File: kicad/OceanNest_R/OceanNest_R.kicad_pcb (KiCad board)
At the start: 2 copper layers, 103.4 x 85.9 mm, 40 parts, among them J21 Conn_01x07_Pin, J22 TRRS_MJ-4PP-9, SW21 SW_PUSH, SW22 SW_PUSH, SW23 SW_PUSH, SW24 SW_PUSH, SW25 SW_PUSH, SW26 SW_PUSH, SW27 SW_PUSH, SW28 SW_PUSH, SW29 SW_PUSH, SW30 SW_PUSH, SW31 SW_PUSH, SW32 SW_PUSH, SW33 SW_PUSH, SW34 SW_PUSH, SW35 SW_PUSH, SW36 SW_PUSH, U21 RP2040-Zero

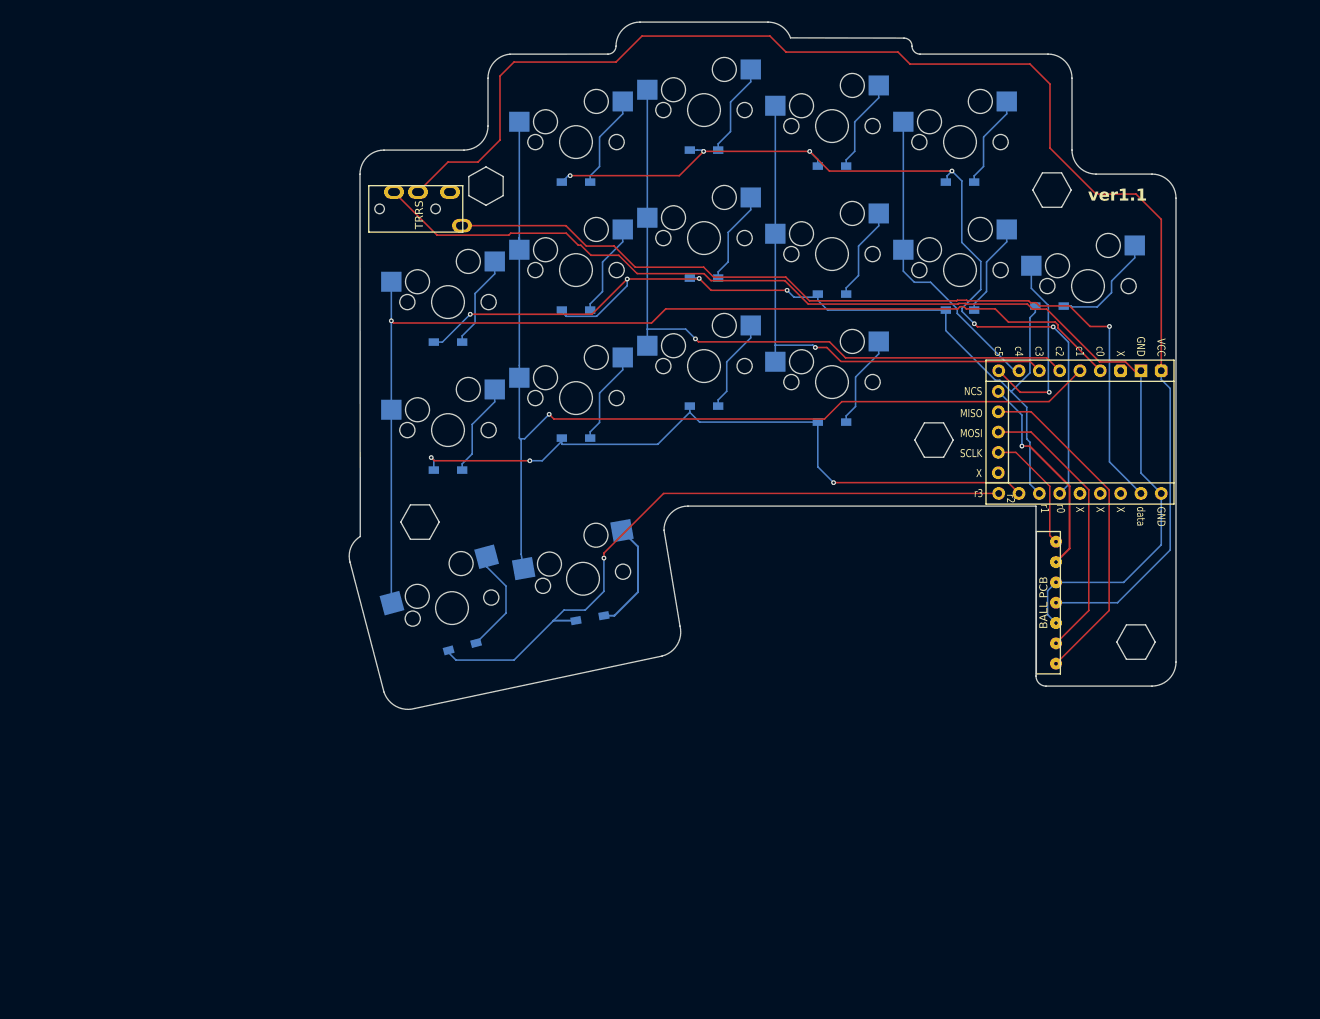
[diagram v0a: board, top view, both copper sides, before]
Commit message: feat: update PCB and schematic files for OceanNest project, including new components and layout adjustments
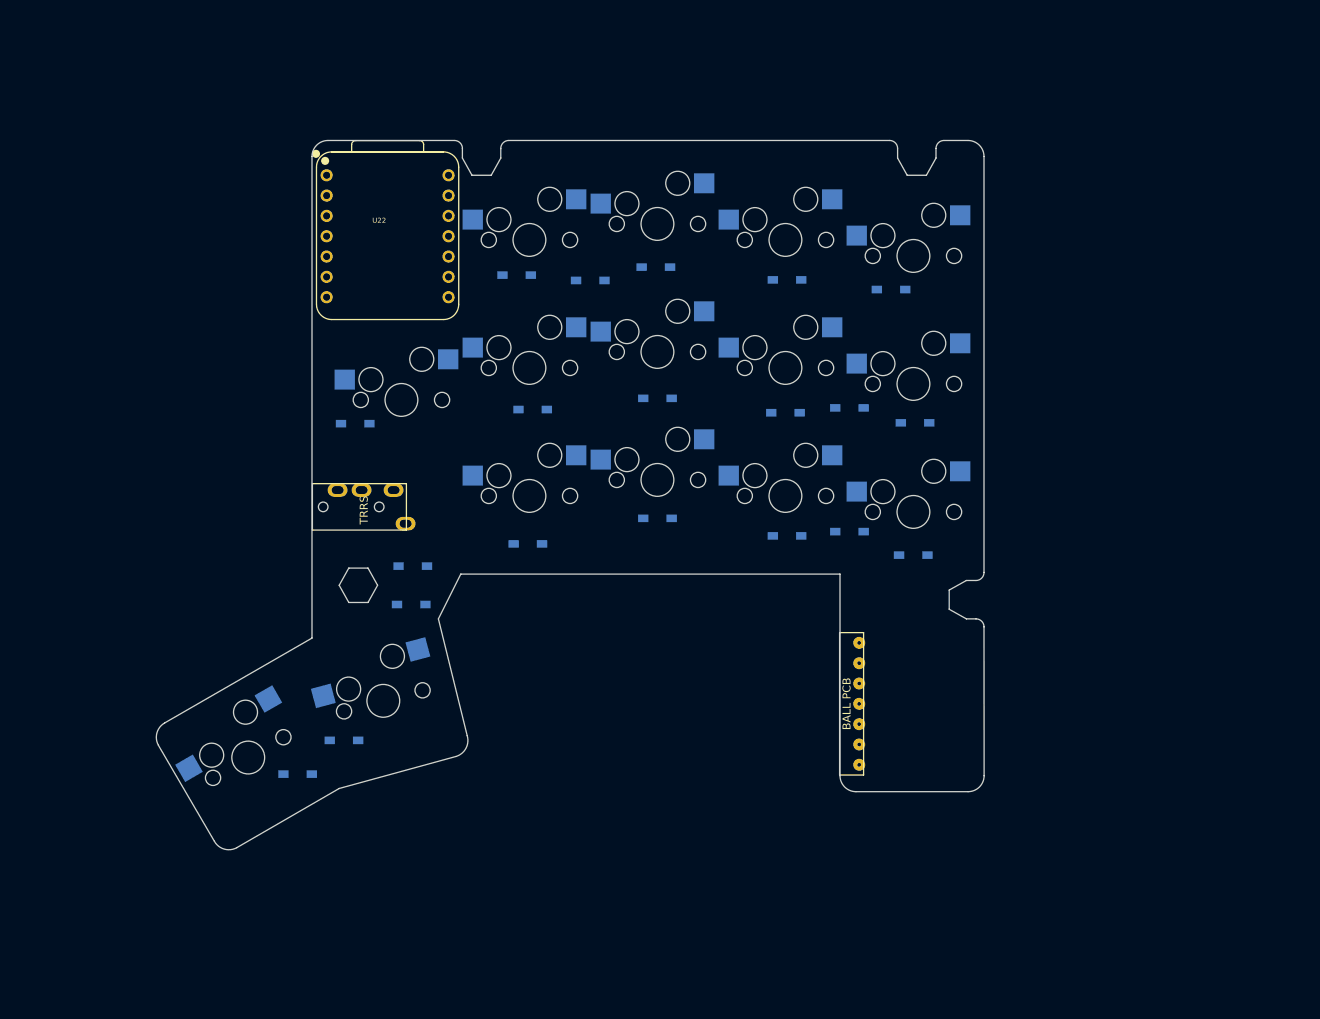
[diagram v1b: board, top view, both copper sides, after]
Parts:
- removed the Ref** at (197.0, 124.5)
- removed the Ref** at (115.8, 67.5)
- removed the Ref** at (171.8, 99.2)
- removed the Ref** at (107.5, 109.5)
- removed the Ref** at (186.5, 68.0)
- removed SW36: SW_PUSH, takashicompany:CherryMX_Hotswap_16m
- removed U21: RP2040-Zero, isw-kbd:RP2040-Zero
- added D37: D, kbd_Parts:Diode_SMD, F.Cu at (169.2, 113.6)
- added D38: D, kbd_Parts:Diode_SMD, F.Cu at (92.2, 141.0)
- added D39: D, kbd_Parts:Diode_SMD, F.Cu at (98.0, 136.8)
- added D40: D, kbd_Parts:Diode_SMD, F.Cu at (106.6, 115.0)
- added Ref**: Val**, kbd_Hole:m2_Spacer_Hole_hex, F.Cu at (99.8, 117.4)
- added U22: XIAO-RP2040-TH, xiao_rp2040:XIAO-RP2040-TH, F.Cu at (103.5, 73.8)
- J21: value Conn_01x07_Pin -> TRRS_MJ-4PP-9; footprint kbd:Mac8_L_7pin_contact_NEW2023 -> kbd:MJ-4PP-9; moved to F.Cu
- J22: value TRRS_MJ-4PP-9 -> Conn_01x07_Pin; footprint kbd:MJ-4PP-9 -> kbd:Mac8_L_7pin_contact_NEW2023; moved to B.Cu
- SW21, SW22, SW23, SW24, SW25, SW26, SW27, SW28, SW29, SW30, SW31, SW32, SW33, SW34, SW35: value SW_PUSH -> SW_Push
- moved J21 94.1 mm to (93.9, 107.6)
- moved J22 87.3 mm to (162.6, 132.2)
- moved SW34 86.8 mm to (86.0, 138.9), turned to 30 degrees
- moved SW30 74.6 mm to (121.2, 106.2)
- moved D25 55.8 mm to (166.4, 80.4)
- moved D27 54.8 mm to (106.4, 119.8)
- moved D35 42.9 mm to (153.4, 111.2), turned to 0 degrees
- moved D31 42.8 mm to (153.2, 95.8)
- moved D32 42.4 mm to (169.4, 97.1)
- moved D28 40.1 mm to (121.6, 95.4)
- moved D29 39.4 mm to (137.2, 94.0)
- moved D36 34.2 mm to (161.2, 110.7), turned to 0 degrees
- moved SW33 31.9 mm to (169.2, 108.2)
- moved D26 31.0 mm to (99.4, 97.2)
- moved SW32 28.9 mm to (153.2, 106.2)
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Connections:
- D21 pad 1: row0 -> Net-(D21-K)
- D21 pad 2: Net-(D21-A) -> pin1
- D22 pad 1: row0 -> pin1
- D23 pad 1: row0 -> pin1
- D24 pad 1: row0 -> pin1
- D25 pad 1: row1 -> pin1
- D26 pad 1: row1 -> pin2
- D27 pad 1: row1 -> Net-(D27-K)
- D27 pad 2: Net-(D27-A) -> pin2
- D28 pad 1: row1 -> pin3
- D29 pad 1: row1 -> pin3
- D30 pad 1: row1 -> Net-(D30-K)
- D30 pad 2: Net-(D30-A) -> pin3
- D31 pad 1: row2 -> pin3
- D32 pad 1: row2 -> pin3
- D33 pad 1: row2 -> pin4
- D34 pad 1: row2 -> pin4
- D35 pad 1: row3 -> pin4
- D36 pad 1: row3 -> Net-(D36-K)
- D36 pad 2: Net-(D36-A) -> pin4
- SW21 pad 1: col1 -> Net-(D27-K)
- SW21 pad 2: Net-(D21-A) -> Net-(D22-A)
- SW22 pad 1: col2 -> Net-(D30-K)
- SW22 pad 2: Net-(D22-A) -> Net-(D23-A)
- SW23 pad 1: col3 -> Net-(D36-K)
- SW23 pad 2: Net-(D23-A) -> Net-(D24-A)
- SW24 pad 1: col4 -> Net-(D40-K)
- SW24 pad 2: Net-(D24-A) -> Net-(D25-A)
- SW25 pad 1: col0 -> Net-(D21-K)
- SW25 pad 2: Net-(D25-A) -> Net-(D26-A)
- SW26 pad 1: col1 -> Net-(D21-K)
- SW26 pad 2: Net-(D26-A) -> Net-(D28-A)
- SW27 pad 1: col2 -> Net-(D27-K)
- SW27 pad 2: Net-(D27-A) -> Net-(D29-A)
- SW28 pad 1: col3 -> Net-(D36-K)
- SW28 pad 2: Net-(D28-A) -> Net-(D31-A)
- SW29 pad 1: col4 -> Net-(D40-K)
- SW29 pad 2: Net-(D29-A) -> Net-(D32-A)
- SW30 pad 1: col5 -> Net-(D21-K)
- SW30 pad 2: Net-(D30-A) -> Net-(D33-A)
- SW31 pad 1: col0 -> Net-(D27-K)
- SW31 pad 2: Net-(D31-A) -> Net-(D34-A)
- SW32 pad 1: col1 -> Net-(D30-K)
- SW32 pad 2: Net-(D32-A) -> Net-(D35-A)
- SW33 pad 1: col2 -> Net-(D40-K)
- SW33 pad 2: Net-(D33-A) -> Net-(D37-A)
- SW34 pad 1: col3 -> Net-(D21-K)
- SW34 pad 2: Net-(D34-A) -> Net-(D38-A)
- SW35 pad 1: col0 -> Net-(D27-K)
- SW35 pad 2: Net-(D35-A) -> Net-(D39-A)
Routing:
- net VCC: track 178.7 -> 0.00 mm
- net GND: track 146.8 -> 0.00 mm
- net col0: track 133.3 -> 0.00 mm, vias 1 -> 0
- net col1: track 131.5 -> 0.00 mm, vias 1 -> 0
- net row1: track 121.8 -> 0.00 mm, vias 4 -> 0
- net row0: track 111.4 -> 0.00 mm, vias 6 -> 0
- net data: track 108.7 -> 0.00 mm, vias 1 -> 0
- net row2: track 87.0 -> 0.00 mm, vias 3 -> 0
- net col2: track 85.7 -> 0.00 mm, vias 1 -> 0
- net row3: track 83.8 -> 0.00 mm, vias 1 -> 0
- net col3: track 66.3 -> 0.00 mm, vias 1 -> 0
- net MISO: track 42.4 -> 0.00 mm
- net col4: track 38.6 -> 0.00 mm
- net MOSI: track 35.2 -> 0.00 mm
- net NCS: track 26.3 -> 0.00 mm, vias 1 -> 0
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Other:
- board size 103.4 x 85.9 mm -> 103.5 x 88.7 mm
- board text removed: "c0"
- board text removed: "ver1.1"

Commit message: feat: add new PCB and schematic files for OceanNest_L and OceanNest_L_Bottom, including layout adjustments and component updates
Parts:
- moved D27 18.4 mm to (105.2, 101.5)
- moved D26 11.0 mm to (110.4, 97.4)
- moved D40 7.44 mm to (111.0, 109.0)
- moved D39 6.01 mm to (104.0, 137.0), turned to 15 degrees
- moved D38 4.39 mm to (88.4, 143.2), turned to 30 degrees
- moved D33 2.08 mm to (120.0, 110.4)
- moved D36 0.91 mm to (161.2, 111.6)
- moved D34 0.69 mm to (136.6, 109.4)
- moved D21 0.42 mm to (129.2, 79.3)
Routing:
- net VCC: track 0.00 -> 231.9 mm
- net MISO: track 0.00 -> 156.5 mm, vias 0 -> 2
- net MOSI: track 0.00 -> 152.9 mm, vias 0 -> 2
- net NCS: track 0.00 -> 149.9 mm, vias 0 -> 2
- net SCLK: track 0.00 -> 146.6 mm, vias 0 -> 2
- net GND: track 0.00 -> 145.1 mm
- net Net-(D21-K): track 0.00 -> 120.4 mm, vias 0 -> 4
- net pin5: track 0.00 -> 114.7 mm, vias 0 -> 4
- net Net-(D27-K): track 0.00 -> 113.4 mm, vias 0 -> 8
- net pin4: track 0.00 -> 112.2 mm, vias 0 -> 4
- net pin3: track 0.00 -> 98.1 mm, vias 0 -> 4
- net Net-(D40-K): track 0.00 -> 93.7 mm, vias 0 -> 4
- net pin1: track 0.00 -> 90.0 mm, vias 0 -> 2
- net Net-(D30-K): track 0.00 -> 76.2 mm, vias 0 -> 2
- net Net-(D36-K): track 0.00 -> 58.2 mm, vias 0 -> 4
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- added copper zone on B.Cu, net GND
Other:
- board text added: "GND"
- board text added: "MISO"
- board text added: "MOSI"
- board text added: "NCS"
- board text added: "OceanNest ver2.0"
- board text added: "SCLK"
- board text added: "VCC"
- board text added: "X"
- board text added: "data"
- board text added: "pin1"
- board text added: "pin2"
- board text added: "pin3"
- board text added: "pin4"
- board text added: "pin5"

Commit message: fix: update filenames and step files in OceanNest project for consistency and clarity
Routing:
- net VCC: track 231.9 -> 138.5 mm, vias 0 -> 2
- net GND: track 145.1 -> 194.4 mm, vias 0 -> 3
- net NCS: track 149.9 -> 105.9 mm, vias 2 -> 7
- net SCLK: track 146.6 -> 105.3 mm, vias 2 -> 3
- net MISO: track 156.5 -> 125.1 mm, vias 2 -> 4
- net MOSI: track 152.9 -> 127.7 mm, vias 2 -> 0
- net data: track 39.9 -> 38.3 mm, vias 2 -> 1
- net Net-(D21-K): track 120.4 -> 119.8 mm
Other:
- board text added: "OceanNest ver2.1"
- board text removed: "OceanNest ver2.0"

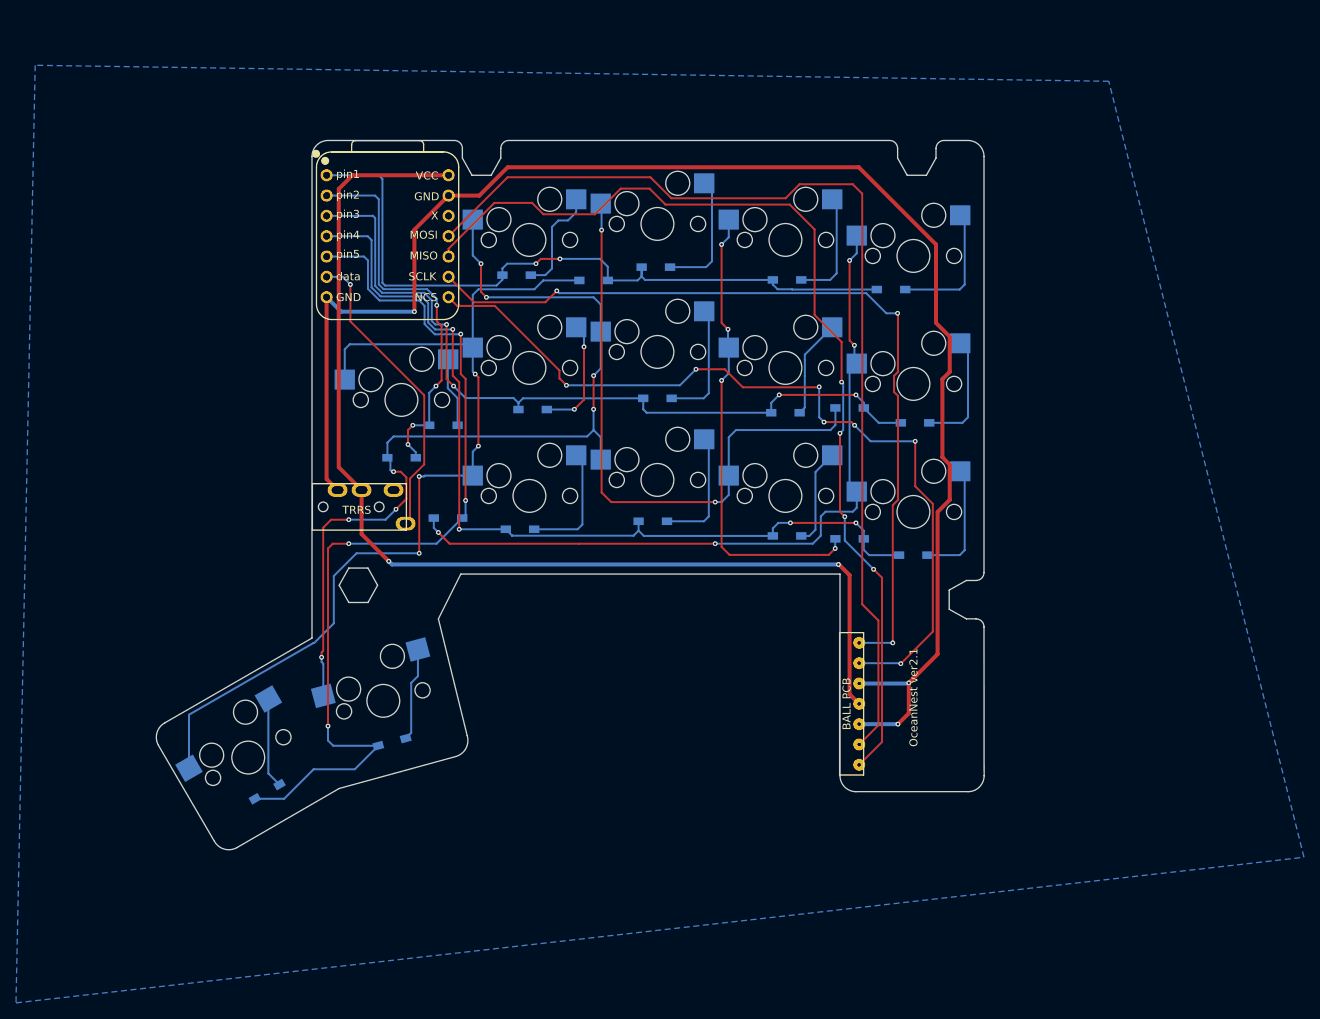
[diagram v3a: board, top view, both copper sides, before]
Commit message: feat: add new OceanNest_L and OceanNest_R PCB and project files for enhanced design capabilities
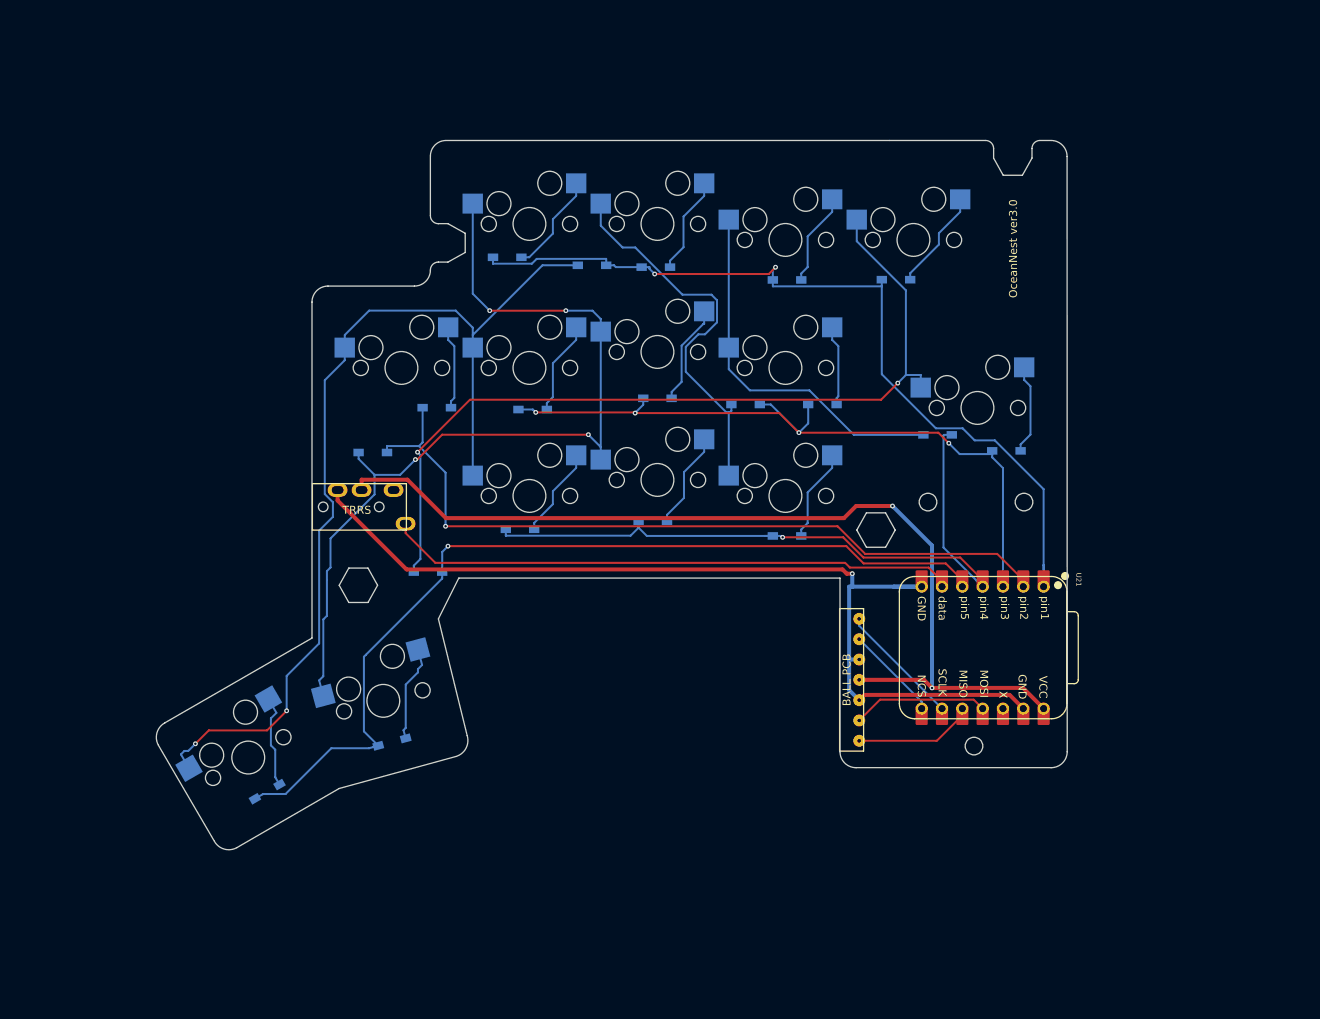
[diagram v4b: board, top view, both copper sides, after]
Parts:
- removed the D37 at (169.2, 113.6)
- removed the SW33 at (169.2, 108.2)
- added hole2: Val**, kbd_Hole:m2_Spacer_Hole_hex, F.Cu at (164.5, 110.5)
- added sc0: Val**, kbd_Hole:m2_Screw_Hole, F.Cu at (171.0, 107.0)
- added sc1: Val**, kbd_Hole:m2_Screw_Hole, F.Cu at (183.0, 107.0)
- added sc2: Val**, kbd_Hole:m2_Screw_Hole, F.Cu at (176.8, 137.5)
- U21: renamed from U22; value XIAO-RP2040-TH -> XIAO-RP2040-DIP; footprint xiao_rp2040:XIAO-RP2040-TH -> xiao_rp2040:XIAO-RP2040-DIP
- moved U21 90.4 mm to (177.8, 125.2), turned to -90 degrees
- moved D36 17.0 mm to (172.2, 98.6)
- moved D30 13.0 mm to (148.2, 94.8)
- moved D32 11.9 mm to (180.8, 100.6)
- moved SW29 8.54 mm to (177.2, 95.2)
- moved D39 7.20 mm to (108.5, 115.8)
- moved D31 4.73 mm to (157.8, 94.8)
- moved SW25 4.00 mm to (105.2, 90.2)
- moved D27 3.66 mm to (101.6, 100.8)
- moved J22 3.00 mm to (162.6, 129.2)
- moved D22 2.52 mm to (118.4, 76.4)
- moved D26 2.35 mm to (109.6, 95.2)
- moved SW21 2.00 mm to (121.2, 72.2)
- moved SW24 2.00 mm to (169.2, 74.2)
- moved D21 1.90 mm to (129.0, 77.4)
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- renumbered D38 to D37, D39 to D38, D40 to D39, SW34 to SW33, SW35 to SW34, Ref** to hole1
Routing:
- net MISO: track 125.1 -> 15.7 mm, vias 4 -> 0
- net MOSI: track 127.7 -> 18.4 mm
- net NCS: track 105.9 -> 13.8 mm, vias 7 -> 0
- net SCLK: track 105.3 -> 16.8 mm, vias 3 -> 0
- net GND: track 194.4 -> 123.8 mm, vias 3 -> 1
- net pin2: track 48.8 -> 97.4 mm, vias 4 -> 1
- net data: track 38.3 -> 72.1 mm, vias 1 -> 0
- net Net-(D30-K): track 76.2 -> 48.8 mm, vias 2 -> 0
- net pin4: track 112.2 -> 89.8 mm, vias 4 -> 1
- net pin1: track 90.0 -> 108.6 mm
- net VCC: track 138.5 -> 120.9 mm
- net Net-(D37-A) (its old number): track 15.0 -> 0.00 mm
- net Net-(D39-K): track 93.7 -> 105.9 mm, vias 4 -> 2
- net Net-(D36-K): track 58.2 -> 46.4 mm, vias 4 -> 0
- net pin3: track 98.1 -> 93.1 mm
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- removed copper zone on B.Cu, net GND
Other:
- board size 103.5 x 88.7 mm -> 113.9 x 88.7 mm
- board text added: "OceanNest ver3.0"
- board text removed: "OceanNest ver2.1"
